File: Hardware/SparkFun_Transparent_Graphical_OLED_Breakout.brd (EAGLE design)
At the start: 25.4 x 25.4 mm, 70 parts, among them U1 AP3012, U2 UG-2856KLBAG01_4WSPI

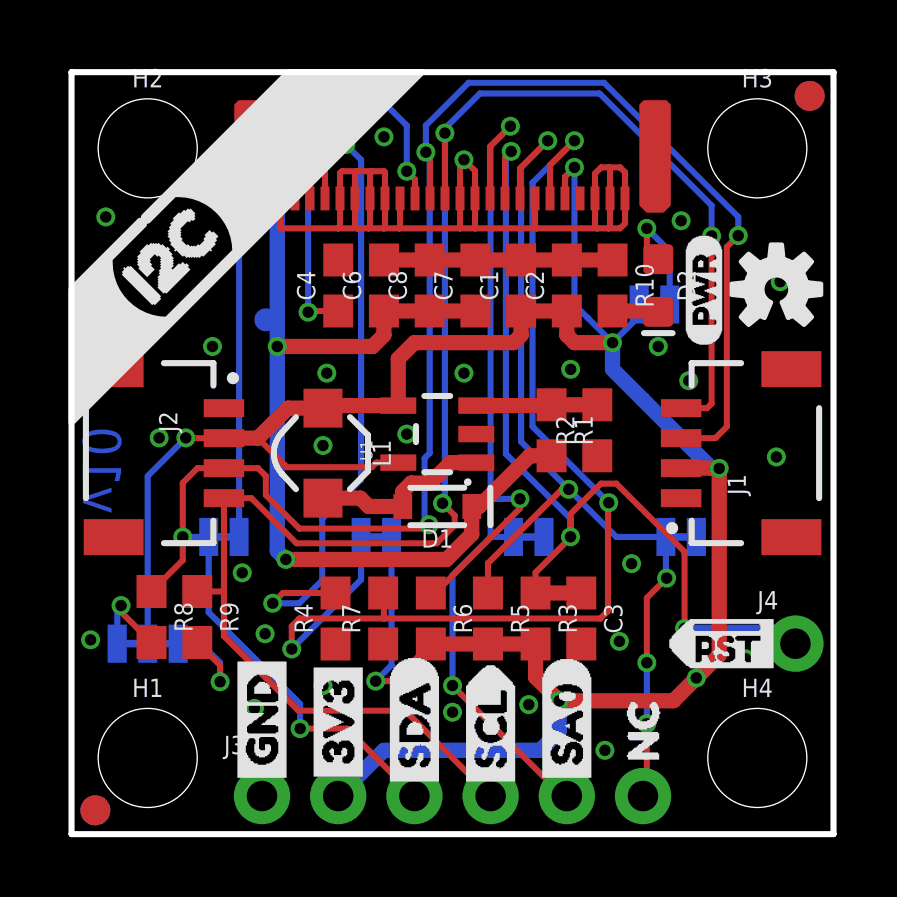
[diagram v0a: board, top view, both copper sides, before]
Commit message: Fix issue #2
Added units to measures
Removed unused via on 3.3V line (lower right)
Widened input 3.3V trace to boost IC to 20 mil
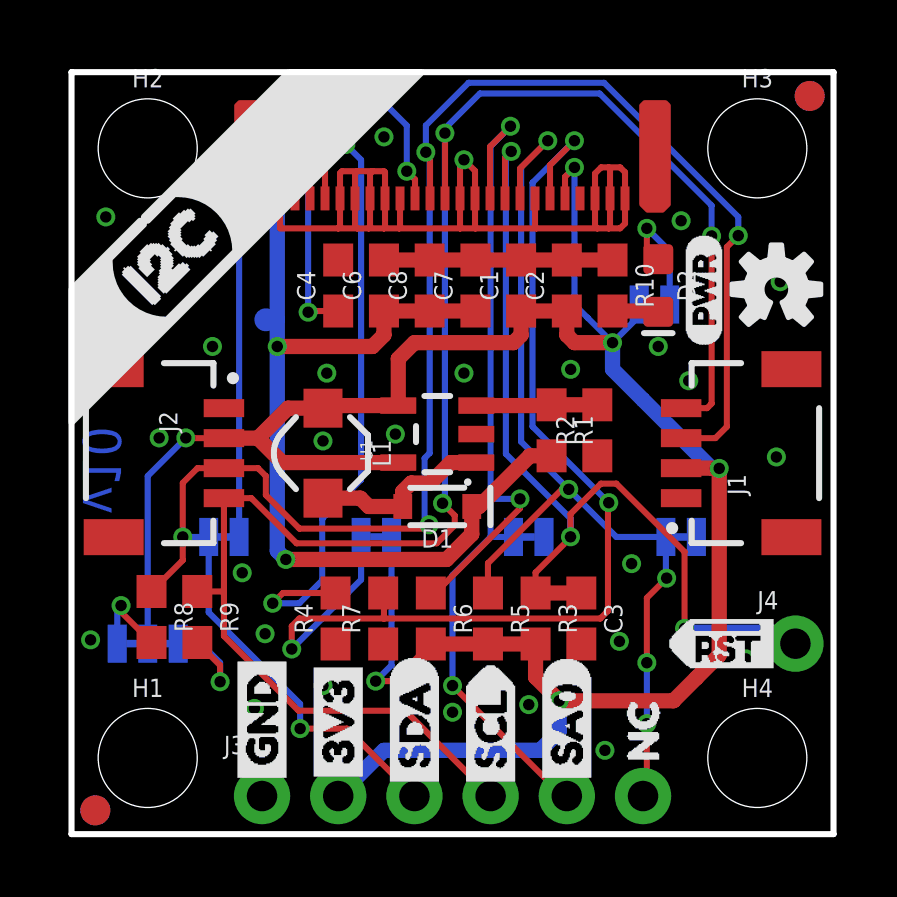
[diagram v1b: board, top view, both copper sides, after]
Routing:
- net 3.3V: track 81.6 -> 81.5 mm, vias 7 -> 6
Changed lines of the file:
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@@
 <setting verticaltext="up"/>
 </settings>
-<grid distance="50" unitdist="mil" unit="mil" style="lines" multiple="1" display="yes" altdistance="1" altunitdist="mil" altunit="mil"/>
+<grid distance="5" unitdist="mil" unit="mil" style="lines" multiple="1" display="yes" altdistance="1" altunitdist="mil" altunit="mil"/>
 <layers>
 <layer number="1" name="Top" color="4" fill="1" visible="yes" active="yes"/>
@@
 <layer number="23" name="tOrigins" color="15" fill="1" visible="yes" active="yes"/>
 <layer number="24" name="bOrigins" color="15" fill="1" visible="yes" active="yes"/>
-<layer number="25" name="tNames" color="7" fill="1" visible="yes" active="yes"/>
-<layer number="26" name="bNames" color="7" fill="1" visible="yes" active="yes"/>
-<layer number="27" name="tValues" color="7" fill="1" visible="yes" active="yes"/>
-<layer number="28" name="bValues" color="7" fill="1" visible="yes" active="yes"/>
-<layer number="29" name="tStop" color="7" fill="3" visible="yes" active="yes"/>
-<layer number="30" name="bStop" color="7" fill="6" visible="yes" active="yes"/>
-<layer number="31" name="tCream" color="7" fill="4" visible="yes" active="yes"/>
-<layer number="32" name="bCream" color="7" fill="5" visible="yes" active="yes"/>
-<layer number="33" name="tFinish" color="6" fill="3" visible="yes" active="yes"/>
-<layer number="34" name="bFinish" color="6" fill="6" visible="yes" active="yes"/>
-<layer number="35" name="tGlue" color="7" fill="4" visible="yes" active="yes"/>
-<layer number="36" name="bGlue" color="7" fill="5" visible="yes" active="yes"/>
-<layer number="37" name="tTest" color="7" fill="1" visible="yes" active="yes"/>
-<layer number="38" name="bTest" color="7" fill="1" visible="yes" active="yes"/>
-<layer number="39" name="tKeepout" color="4" fill="11" visible="yes" active="yes"/>
-<layer number="40" name="bKeepout" color="1" fill="11" visible="yes" active="yes"/>
-<layer number="41" name="tRestrict" color="4" fill="10" visible="yes" active="yes"/>
-<layer number="42" name="bRestrict" color="1" fill="10" visible="yes" active="yes"/>
-<layer number="43" name="vRestrict" color="2" fill="10" visible="yes" active="yes"/>
-<layer number="44" name="Drills" color="7" fill="1" visible="yes" active="yes"/>
+<layer number="25" name="tNames" color="7" fill="1" visible="no" active="yes"/>
+<layer number="26" name="bNames" color="7" fill="1" visible="no" active="yes"/>
+<layer number="27" name="tValues" color="7" fill="1" visible="no" active="yes"/>
+<layer number="28" name="bValues" color="7" fill="1" visible="no" active="yes"/>
+<layer number="29" name="tStop" color="7" fill="3" visible="no" active="yes"/>
+<layer number="30" name="bStop" color="7" fill="6" visible="no" active="yes"/>
+<layer number="31" name="tCream" color="7" fill="4" visible="no" active="yes"/>
+<layer number="32" name="bCream" color="7" fill="5" visible="no" active="yes"/>
+<layer number="33" name="tFinish" color="6" fill="3" visible="no" active="yes"/>
+<layer number="34" name="bFinish" color="6" fill="6" visible="no" active="yes"/>
+<layer number="35" name="tGlue" color="7" fill="4" visible="no" active="yes"/>
+<layer number="36" name="bGlue" color="7" fill="5" visible="no" active="yes"/>
+<layer number="37" name="tTest" color="7" fill="1" visible="no" active="yes"/>
+<layer number="38" name="bTest" color="7" fill="1" visible="no" active="yes"/>
+<layer number="39" name="tKeepout" color="4" fill="11" visible="no" active="yes"/>
+<layer number="40" name="bKeepout" color="1" fill="11" visible="no" active="yes"/>
+<layer number="41" name="tRestrict" color="4" fill="10" visible="no" active="yes"/>
+<layer number="42" name="bRestrict" color="1" fill="10" visible="no" active="yes"/>
+<layer number="43" name="vRestrict" color="2" fill="10" visible="no" active="yes"/>
+<layer number="44" name="Drills" color="7" fill="1" visible="no" active="yes"/>
 <layer number="45" name="Holes" color="7" fill="1" visible="yes" active="yes"/>
-<layer number="46" name="Milling" color="3" fill="1" visible="yes" active="yes"/>
+<layer number="46" name="Milling" color="3" fill="1" visible="no" active="yes"/>
 <layer number="47" name="Measures" color="7" fill="1" visible="yes" active="yes"/>
-<layer number="48" name="Document" color="7" fill="1" visible="yes" active="yes"/>
-<layer number="49" name="Reference" color="7" fill="1" visible="yes" active="yes"/>
-<layer number="50" name="dxf" color="7" fill="1" visible="yes" active="yes"/>
+<layer number="48" name="Document" color="7" fill="1" visible="no" active="yes"/>
+<layer number="49" name="Reference" color="7" fill="1" visible="no" active="yes"/>
+<layer number="50" name="dxf" color="7" fill="1" visible="no" active="yes"/>
 <layer number="51" name="tDocu" color="6" fill="1" visible="yes" active="yes"/>
-<layer number="52" name="bDocu" color="7" fill="1" visible="yes" active="yes"/>
+<layer number="52" name="bDocu" color="7" fill="1" visible="no" active="yes"/>
 <layer number="91" name="Nets" color="2" fill="1" visible="no" active="no"/>
 <layer number="92" name="Busses" color="1" fill="1" visible="no" active="no"/>
@@
 <vertex x="25.4" y="13.716"/>
 </polygon>
-<dimension x1="22.86" y1="22.86" x2="22.86" y2="2.54" x3="30.48" y3="12.7" textsize="1.778" textratio="15" layer="47" unit="inch"/>
-<dimension x1="25.4" y1="25.4" x2="25.4" y2="0" x3="35.56" y3="12.7" textsize="1.778" textratio="15" layer="47" unit="inch"/>
-<dimension x1="2.54" y1="22.86" x2="22.86" y2="22.86" x3="12.7" y3="34.29" textsize="1.778" textratio="15" layer="47" unit="inch"/>
-<dimension x1="0" y1="25.4" x2="25.4" y2="25.4" x3="12.7" y3="39.37" textsize="1.778" textratio="15" layer="47" unit="inch"/>
+<dimension x1="22.86" y1="22.86" x2="22.86" y2="2.54" x3="30.48" y3="12.7" textsize="1.778" textratio="15" layer="47" unit="inch" visible="yes"/>
+<dimension x1="25.4" y1="25.4" x2="25.4" y2="0" x3="35.56" y3="12.7" textsize="1.778" textratio="15" layer="47" unit="inch" visible="yes"/>
+<dimension x1="2.54" y1="22.86" x2="22.86" y2="22.86" x3="12.7" y3="34.29" textsize="1.778" textratio="15" layer="47" unit="inch" visible="yes"/>
+<dimension x1="0" y1="25.4" x2="25.4" y2="25.4" x3="12.7" y3="39.37" textsize="1.778" textratio="15" layer="47" unit="inch" visible="yes"/>
 <wire x1="38.1" y1="12.7" x2="50.8" y2="12.7" width="0.2032" layer="47" style="dashdot"/>
 <wire x1="12.7" y1="43.18" x2="12.7" y2="54.61" width="0.2032" layer="47" style="dashdot"/>
@@
 <wire x1="17.95" y1="21.19" x2="17.95" y2="22.182" width="0.2032" layer="1"/>
 <wire x1="17.95" y1="22.182" x2="17.907" y2="22.225" width="0.2032" layer="1"/>
-<via x="11.176" y="13.335" extent="1-16" drill="0.381"/>
+<via x="10.795" y="13.335" extent="1-16" drill="0.381"/>
 <via x="15.24" y="4.318" extent="1-16" drill="0.381"/>
-<via x="8.382" y="12.954" extent="1-16" drill="0.381"/>
+<via x="8.382" y="13.1064" extent="1-16" drill="0.381"/>
 <via x="8.509" y="15.367" extent="1-16" drill="0.381"/>
 <via x="8.382" y="4.953" extent="1-16" drill="0.381"/>
@@
 <wire x1="8.467" y1="14.285" x2="8.382" y2="14.2" width="0.508" layer="1"/>
 <wire x1="8.382" y1="14.2" x2="7.215" y2="14.2" width="0.508" layer="1"/>
-<wire x1="10.16" y1="12.385" x2="10.8919" y2="12.385" width="0.2032" layer="1"/>
-<wire x1="6.215" y1="13.2" x2="7.184" y2="12.231" width="0.2032" layer="1"/>
-<wire x1="10.006" y1="12.231" x2="10.16" y2="12.385" width="0.2032" layer="1"/>
-<wire x1="7.184" y1="12.231" x2="10.006" y2="12.231" width="0.2032" layer="1"/>
 <wire x1="10.8919" y1="14.285" x2="10.8919" y2="15.8449" width="0.508" layer="1"/>
 <wire x1="10.8919" y1="15.8449" x2="11.43" y2="16.383" width="0.508" layer="1"/>
@@
 <wire x1="16.256" y1="4.445" x2="16.256" y2="3.429" width="0.508" layer="16"/>
 <via x="16.256" y="4.445" extent="1-16" drill="0.381"/>
-<via x="20.828" y="5.207" extent="1-16" drill="0.381"/>
 <wire x1="16.256" y1="4.445" x2="20.066" y2="4.445" width="0.508" layer="1"/>
 <wire x1="20.066" y1="4.445" x2="20.828" y2="5.207" width="0.508" layer="1"/>
@@
 <wire x1="16.51" y1="16.637" x2="16.51" y2="17.438" width="0.508" layer="1"/>
 <wire x1="16.764" y1="16.383" x2="16.51" y2="16.637" width="0.508" layer="1"/>
+<wire x1="10.8919" y1="12.385" x2="7.03" y2="12.385" width="0.508" layer="1"/>
+<wire x1="7.03" y1="12.385" x2="6.215" y2="13.2" width="0.508" layer="1"/>
 </signal>
 <signal name="12V">

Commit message: Add External Display Indicator to help avoid BOM issues
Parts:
- added U$26: EXTERNAL_DISP-UG-2856KLBAG01, SparkFun-Displays:EXT_DISP
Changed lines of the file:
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@@
 <element name="U$22" library="buzzard_labels" package="17" value="" x="21.971" y="24.384" rot="MR0"/>
 <element name="U$23" library="buzzard_labels" package="248" value="" x="6.985" y="24.384" rot="MR0"/>
+<element name="U$26" library="SparkFun-Displays" package="EXT_DISP" value="EXTERNAL_DISP-UG-2856KLBAG01" x="-19.05" y="-15.24"/>
 </elements>
 <signals>
